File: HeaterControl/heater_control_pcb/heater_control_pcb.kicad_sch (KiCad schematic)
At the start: 24 parts, among them J2 I2C, J3 SWD, J4 OUTPUT, Q1 RFP30N06LE, Q2 RFP30N06LE, Q3 RFP30N06LE, Q4 RFP30N06LE, U1 Pico, U2 LM1117DT-3.3

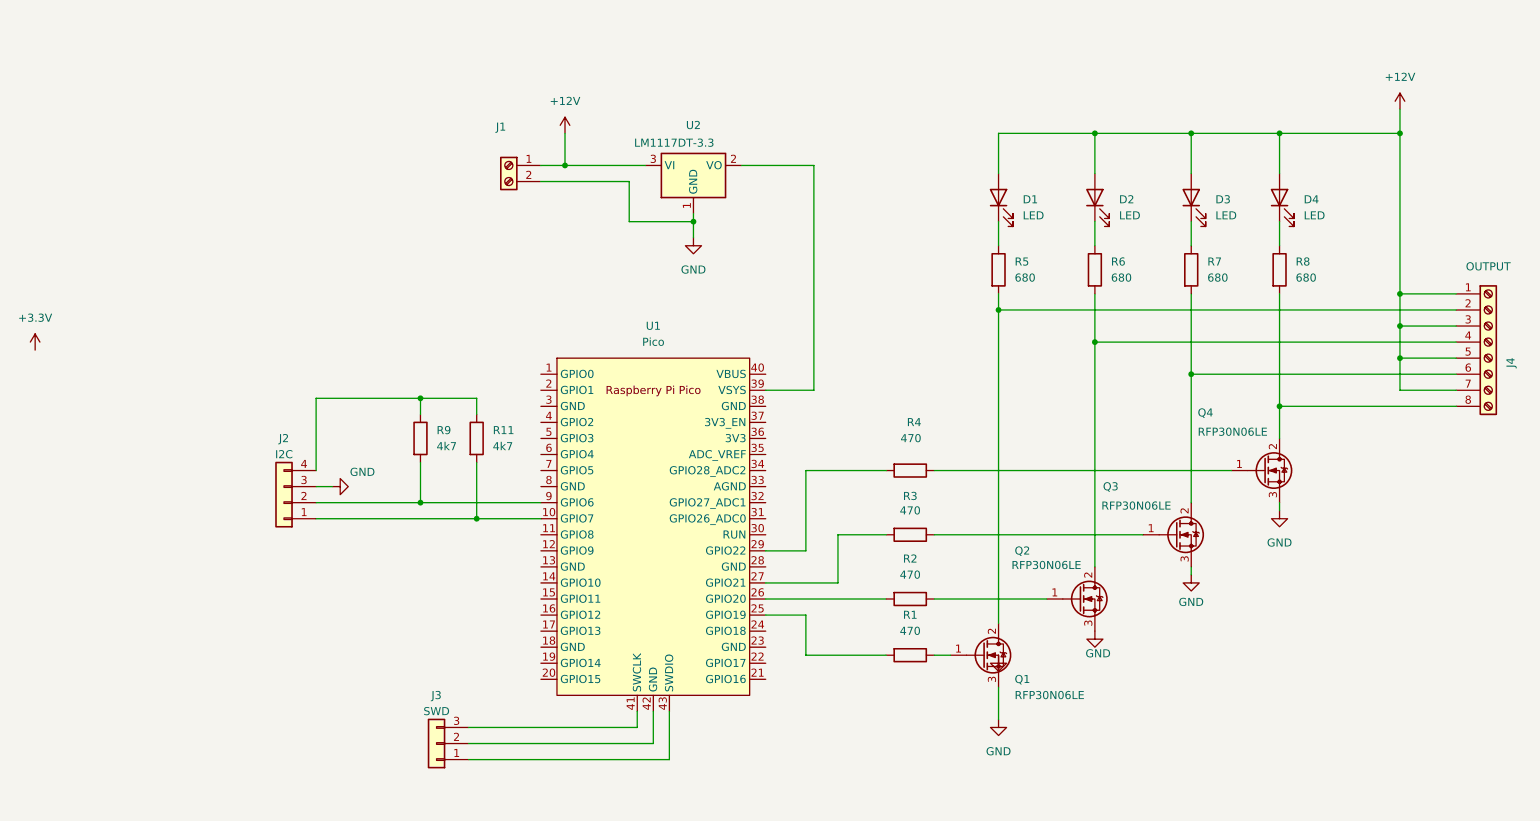
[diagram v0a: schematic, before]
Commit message: Added a test version for the heater firmware
Just turns on all the MOSFETs.

The firmwar works but it looks like I wired in the LEDs reverse
polarity so the circuit can't work doh! (Desoldering is no fun)
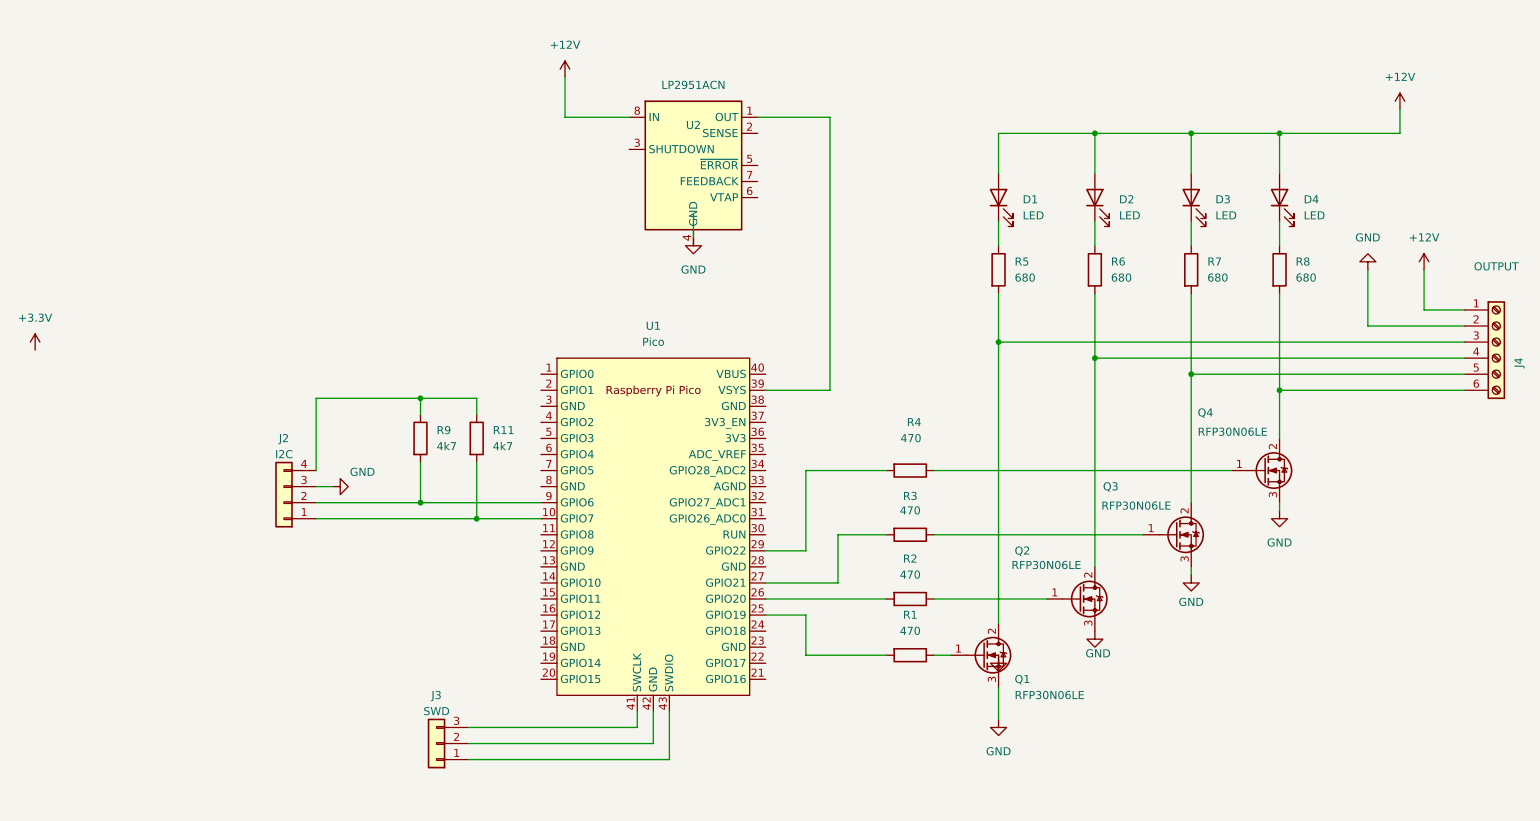
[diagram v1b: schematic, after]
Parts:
- removed J1: ~, TerminalBlock_Phoenix:TerminalBlock_Phoenix_PT-1,5-2-5.0-H_1x02_P5.00mm_Horizontal, symbol Connector:Screw_Terminal_01x02
- J4: footprint TerminalBlock_Phoenix:TerminalBlock_Phoenix_PT-1,5-8-5.0-H_1x08_P5.00mm_Horizontal -> TerminalBlock_Phoenix:TerminalBlock_Phoenix_PT-1,5-6-5.0-H_1x06_P5.00mm_Horizontal; symbol Connector:Screw_Terminal_01x08 -> Connector:Screw_Terminal_01x06
- U2: value LM1117DT-3.3 -> LP2951ACN; footprint Package_TO_SOT_SMD:TO-252-3_TabPin2 -> Package_SO:SOIC-8_3.9x4.9mm_P1.27mm; symbol Regulator_Linear:LM1117DT-5.0 -> Regulator_Linear:LP2951-3.3_SOIC
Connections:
- net +12V: now also U2.8 (IN); no longer J4.3 (Pin_3), J4.5 (Pin_5), J4.7 (Pin_7), U2.3 (VI)
- net GND: now also J4.2 (Pin_2); no longer U2.1 (GND)
- net at Q1.2 (D), R5.2: now also J4.3 (Pin_3); no longer J4.2 (Pin_2)
- net at Q3.2 (D), R7.2: now also J4.5 (Pin_5); no longer J4.6 (Pin_6)
- net at Q4.2 (D), R8.2: now also J4.6 (Pin_6); no longer J4.8 (Pin_8)
- net at U1.39 (VSYS): now also U2.1 (OUT); no longer U2.2 (VO)

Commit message: Update schematics to match prototype
- Added some signal diodes to act as power supply protection:
  - On the 3v3 line on the i2c bus, this drops the voltage to 2v8 but this
    seems to be adeqaute for the TMP117.
  - Between the Pico and the LM7805 to prevent backfeeding the regulator
    when the power isn't connected but the USB bus is.

Used 1n4148 because I have a ton of them - not ideal in terms of
voltage drop on the i2c bus and they can't handle any significant current
but since we're just driving a couple of LEDs it will do for now.
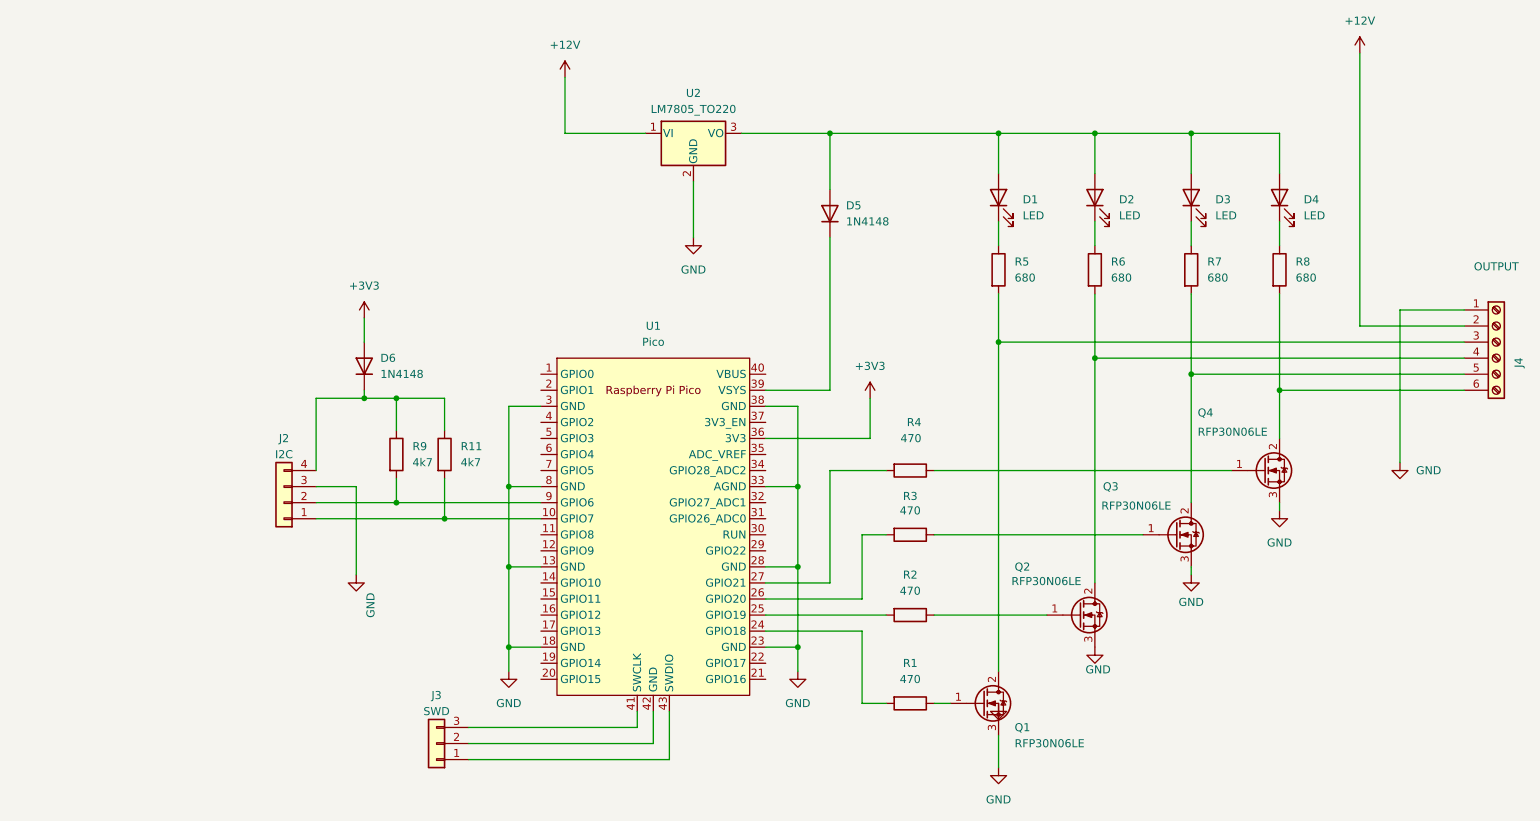
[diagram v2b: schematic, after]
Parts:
- removed U2: LP2951ACN, Package_SO:SOIC-8_3.9x4.9mm_P1.27mm, symbol Regulator_Linear:LP2951-3.3_SOIC
- added D5, D6: 1N4148, Diode_THT:D_DO-35_SOD27_P7.62mm_Horizontal, symbol Diode:1N4148
- added U2: LM7805_TO220, Package_TO_SOT_THT:TO-220-3_Vertical, symbol Regulator_Linear:LM7805_TO220
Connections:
- net +12V: now also J4.2 (Pin_2), U2.1 (VI); no longer D1.2 (A), D2.2 (A), D3.2 (A), D4.2 (A), J4.1 (Pin_1)
- net GND: now also J4.1 (Pin_1), U1.13 (GND), U1.18 (GND), U1.23 (GND), U1.28 (GND), U1.3 (GND), U1.33 (AGND), U1.38 (GND), U1.8 (GND), U2.2 (GND); no longer J4.2 (Pin_2)
- net at R3.2: now also U1.26 (GPIO20); no longer U1.27 (GPIO21)
- net at R4.2: now also U1.27 (GPIO21); no longer U1.29 (GPIO22)
- net at J2.4 (Pin_4), R11.1, R9.1: now also D6.1 (K)
- net at R1.2: now also U1.24 (GPIO18); no longer U1.25 (GPIO19)
- net at R2.2: now also U1.25 (GPIO19); no longer U1.26 (GPIO20)
- net +3V3: now reaches U1.36 (3V3)
- net +3V3: now also D6.2 (A)
- net at U1.39 (VSYS): now also D5.1 (K)
- new net: D1.2 (A), D2.2 (A), D3.2 (A), D4.2 (A), D5.2 (A), U2.3 (VO)
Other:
- moved on the sheet: Q1, Q2, R1, R11, R2, R9

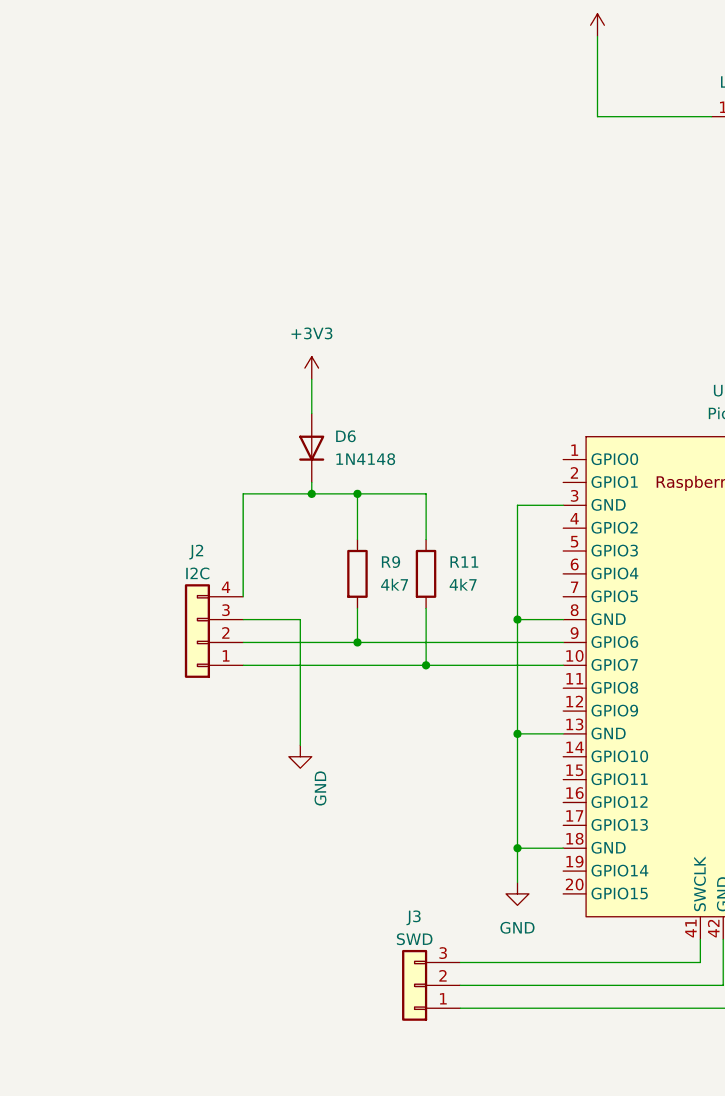
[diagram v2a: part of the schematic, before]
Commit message: We need a second i2c bus!
Multi-master on i2c should in theory work but it looks like the hardware
and software is pretty much configured to assume one master out of the
box.

To avoid the complications the easiet way forward is to add a 2nd i2c
port which is a slave.

So we have:

|RPI octoprint| -> i2c 0 -> |driver board| -> i2c 1 -> |tmp117|

The slave i2c port can be used to set the set point, configure the PID
parameters and read the current value of the TMP117.
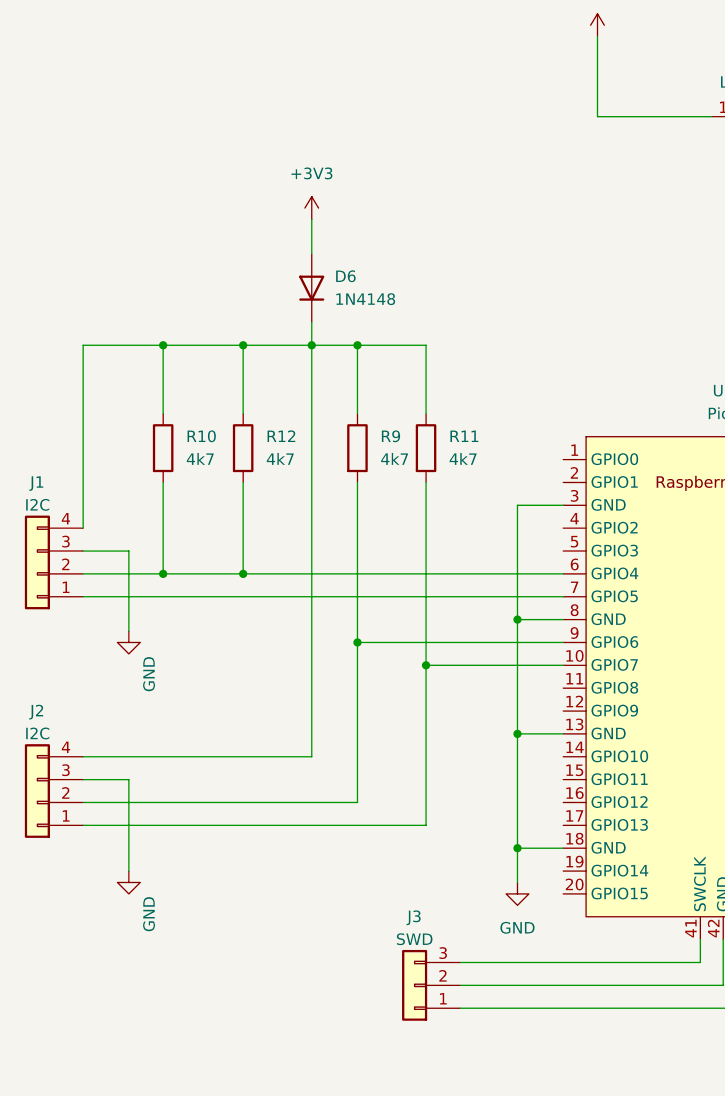
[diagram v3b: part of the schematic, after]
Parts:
- added J1: I2C, Connector_JST:JST_SH_SM04B-SRSS-TB_1x04-1MP_P1.00mm_Horizontal, symbol Connector_Generic:Conn_01x04
- added R10, R12: 4k7, Resistor_THT:R_Axial_DIN0204_L3.6mm_D1.6mm_P5.08mm_Horizontal, symbol Device:R
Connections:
- net GND: now also J1.3 (Pin_3)
- net at D6.1 (K), J2.4 (Pin_4), R11.1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: now also J1.4 (Pin_4), R10.1, R12.1
- net at U1.6 (GPIO4): now also J1.2 (Pin_2), R10.2, R12.2
- net at U1.7 (GPIO5): now also J1.1 (Pin_1)
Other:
- moved on the sheet: D6, J2, R11, R9
